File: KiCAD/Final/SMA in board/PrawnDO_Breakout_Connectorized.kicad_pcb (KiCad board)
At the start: 2 copper layers, 113 x 86.8 mm, 83 parts, among them IC1 74LVT245D,118, IC2 74LVT245D,118, IC3 74LVT245D,118, IC4 74LVT245D,118, J1 do15, J10 do6, J11 do5, J12 do4, J13 do3, J14 do2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

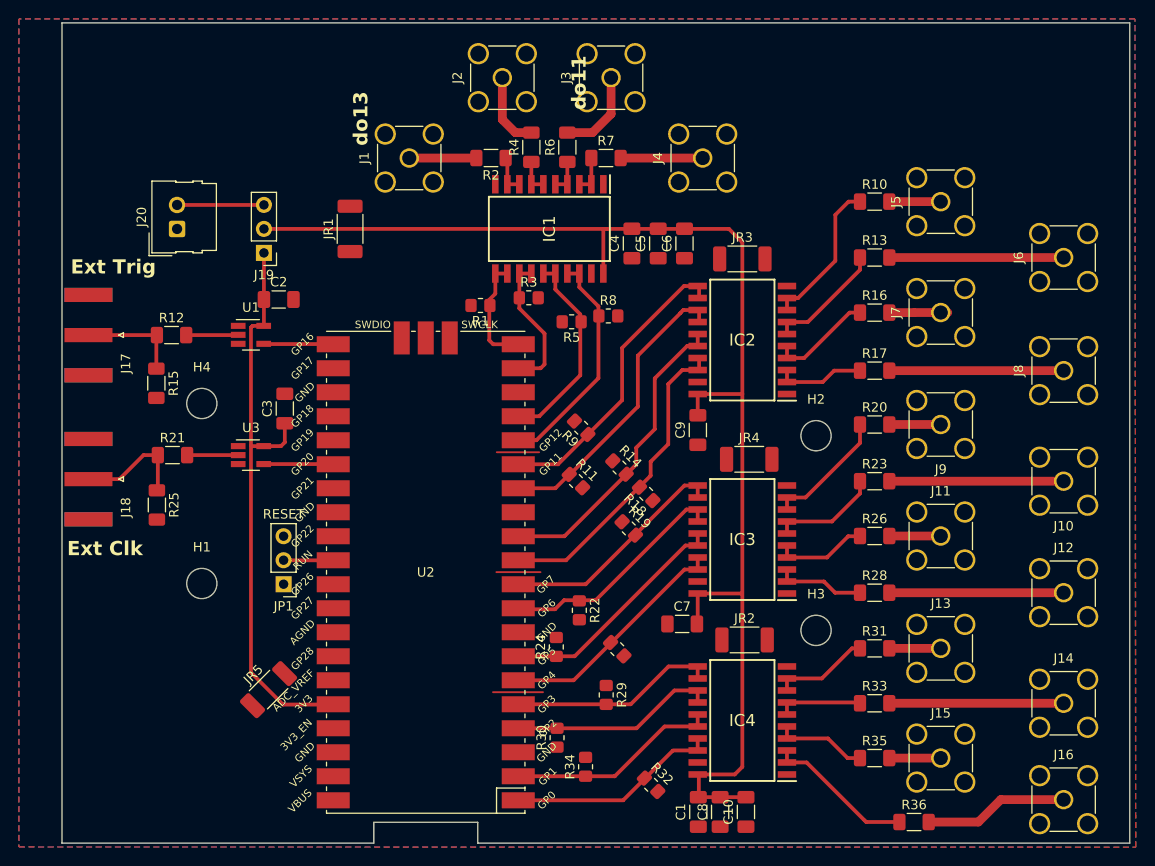
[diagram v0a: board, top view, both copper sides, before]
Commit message: Clean up
Deleted most files/folders

Cleaned up silkscreen and f.fab layers
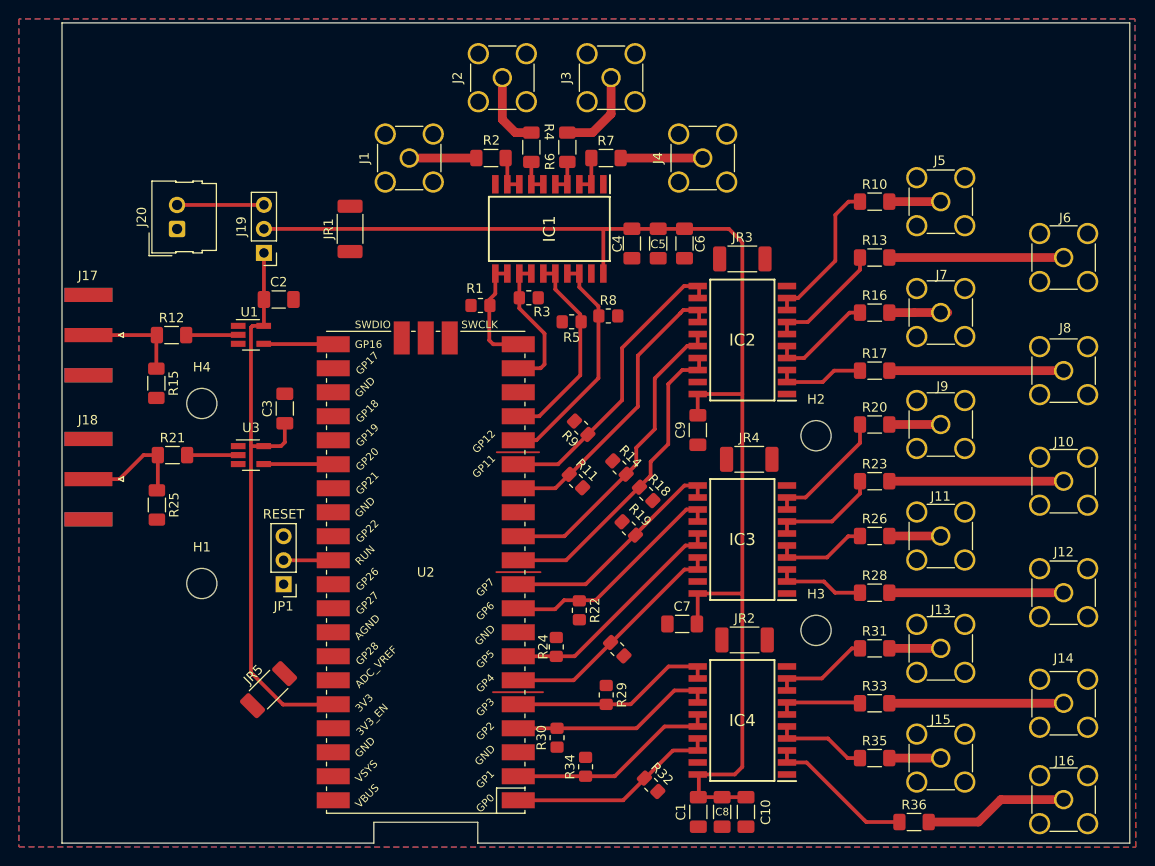
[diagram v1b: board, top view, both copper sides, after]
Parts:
- moved C8 0.21 mm to (141.8, 137.7)
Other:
- board text removed: "do11"
